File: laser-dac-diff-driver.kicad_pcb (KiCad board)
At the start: 2 copper layers, 51 parts, among them IC401 DCDC-CONV_TRACO_TMH-XXXX_Dual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, P101 CONN_2, P102 CONN_3X2, P103 CONN_6X2, U101 AD5689RARUZ, U102 74HC04, U201 OP470, U202 LM358, U401 LM317EMP, U402 LM317EMP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

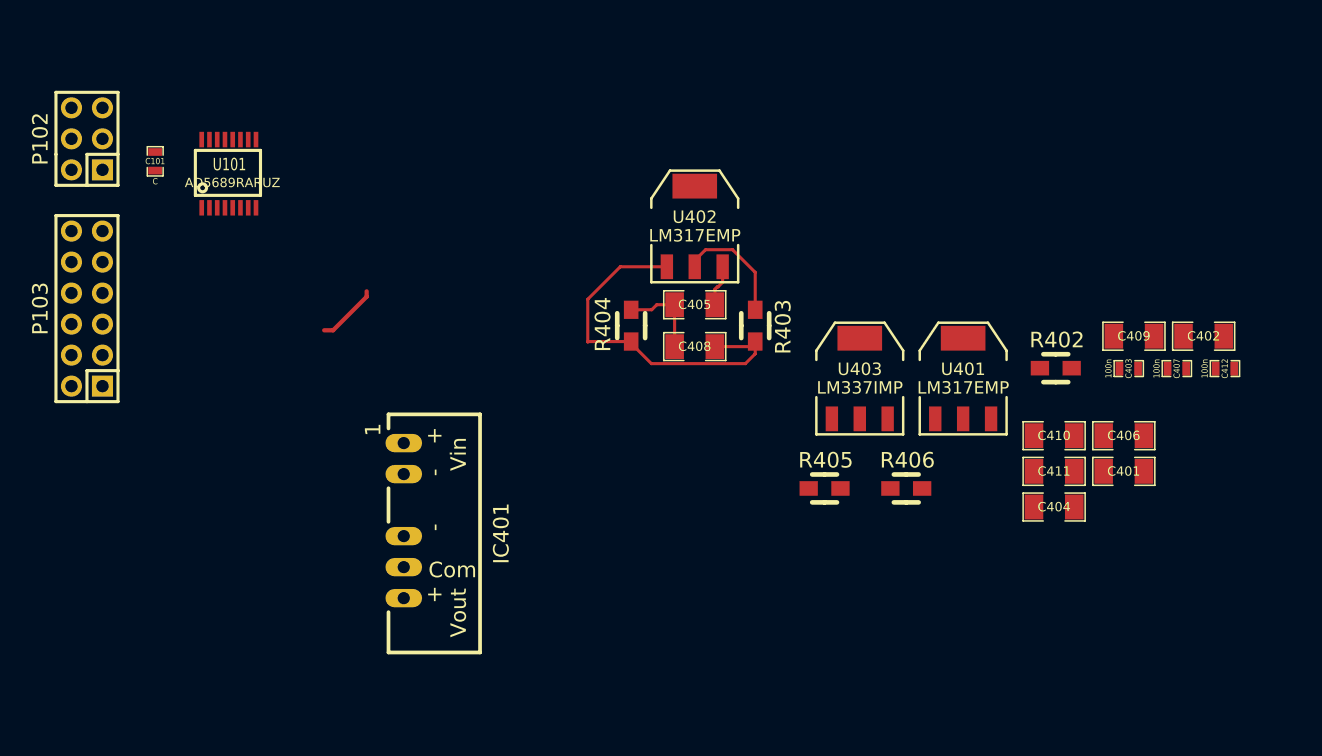
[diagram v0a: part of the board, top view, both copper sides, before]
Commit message: Power supply position changes
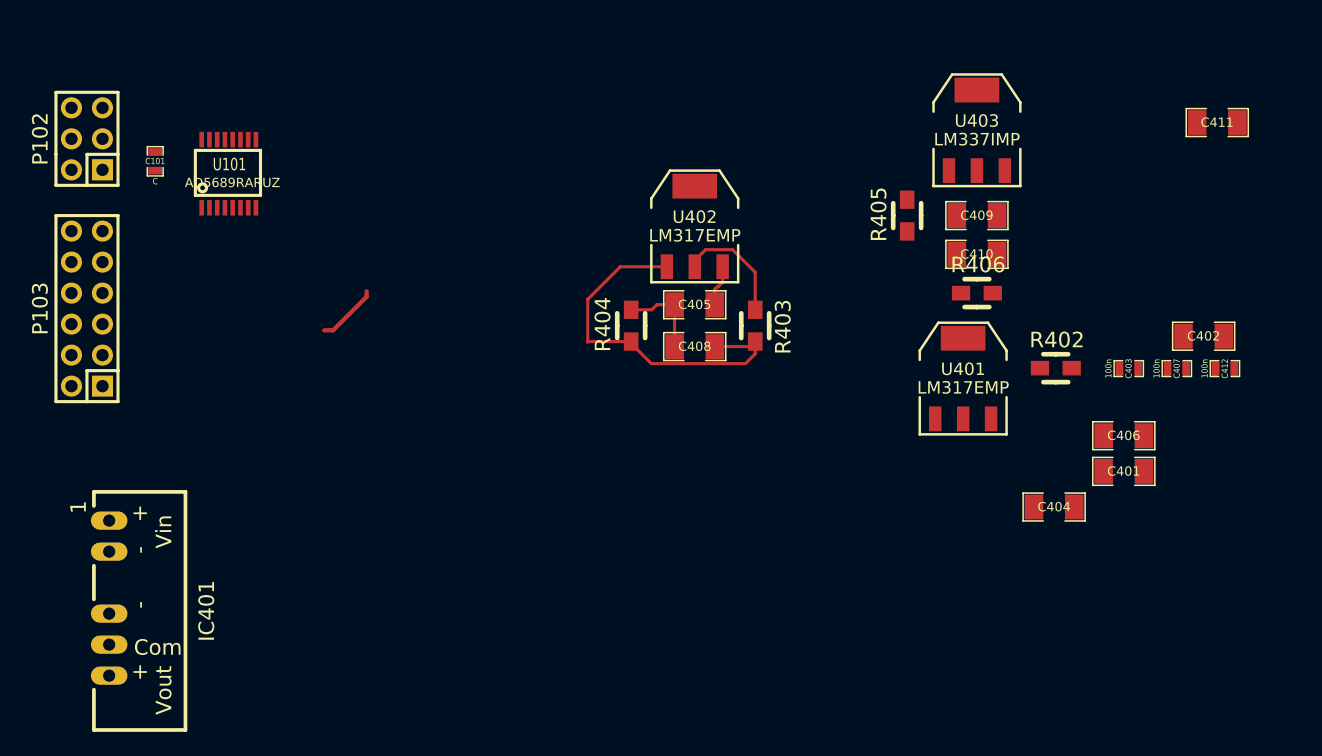
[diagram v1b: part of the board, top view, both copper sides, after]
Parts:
- moved C411 31.5 mm to (215.9, 94.0)
- moved IC401 25.0 mm to (127.6, 134.0)
- moved R405 23.4 mm to (190.5, 101.6), turned to 90 degrees
- moved U403 22.5 mm to (196.2, 94.6)
- moved R406 17.0 mm to (196.2, 108.0)
- moved C409 16.2 mm to (196.2, 101.6), turned to 180 degrees
- moved C410 16.1 mm to (196.2, 104.8)
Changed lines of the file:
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@@
     (pad_to_mask_clearance 0.2)
     (aux_axis_origin 0 0)
-    (visible_elements 7FFFFFFF)
+    (visible_elements 7FFFFFBF)
     (pcbplotparams
       (layerselection 3178497)
@@
   )
   (module SMD_Packages:SM1206 (layer F.Cu)
-    (at 209.077001 111.481501)
-    (attr smd)
-    (fp_text reference C409 (at 0 0) (layer F.SilkS)
-      (effects (font (size 0.762 0.762) (thickness 0.127)))
-    )
-    (fp_text value 10u (at 0 0) (layer F.SilkS) hide
+    (at 196.215 101.6 180)
+    (attr smd)
+    (fp_text reference C409 (at 0 0 180) (layer F.SilkS)
+      (effects (font (size 0.762 0.762) (thickness 0.127)))
+    )
+    (fp_text value 10u (at 0 0 180) (layer F.SilkS) hide
+      (effects (font (size 0.762 0.762) (thickness 0.127)))
+    )
+    (fp_line (start -2.54 -1.143) (end -2.54 1.143) (layer F.SilkS) (width 0.127))
+    (fp_line (start -2.54 1.143) (end -0.889 1.143) (layer F.SilkS) (width 0.127))
+    (fp_line (start 0.889 -1.143) (end 2.54 -1.143) (layer F.SilkS) (width 0.127))
+    (fp_line (start 2.54 -1.143) (end 2.54 1.143) (layer F.SilkS) (width 0.127))
+    (fp_line (start 2.54 1.143) (end 0.889 1.143) (layer F.SilkS) (width 0.127))
+    (fp_line (start -0.889 -1.143) (end -2.54 -1.143) (layer F.SilkS) (width 0.127))
+    (pad 1 smd rect (at -1.651 0 180) (size 1.524 2.032) (layers F.Cu F.Paste F.Mask)
+      (net 22 AGND))
+    (pad 2 smd rect (at 1.651 0 180) (size 1.524 2.032) (layers F.Cu F.Paste F.Mask)
+      (net 26 "Net-(C409-Pad2)"))
+    (model smd/chip_cms.wrl
+      (at (xyz 0 0 0))
+      (scale (xyz 0.17 0.16 0.16))
+      (rotate (xyz 0 0 0))
+    )
+  )
+  (module SMD_Packages:SM1206 (layer F.Cu)
+    (at 196.215 104.775)
+    (attr smd)
+    (fp_text reference C410 (at 0 0) (layer F.SilkS)
+      (effects (font (size 0.762 0.762) (thickness 0.127)))
+    )
+    (fp_text value 1u (at 0 0) (layer F.SilkS) hide
       (effects (font (size 0.762 0.762) (thickness 0.127)))
     )
@@
       (net 22 AGND))
     (pad 2 smd rect (at 1.651 0) (size 1.524 2.032) (layers F.Cu F.Paste F.Mask)
-      (net 26 "Net-(C409-Pad2)"))
+      (net 27 "Net-(C410-Pad2)"))
     (model smd/chip_cms.wrl
       (at (xyz 0 0 0))
@@
   )
   (module SMD_Packages:SM1206 (layer F.Cu)
-    (at 202.537001 119.631501)
-    (attr smd)
-    (fp_text reference C410 (at 0 0) (layer F.SilkS)
+    (at 215.9 93.98)
+    (attr smd)
+    (fp_text reference C411 (at 0 0) (layer F.SilkS)
       (effects (font (size 0.762 0.762) (thickness 0.127)))
     )
@@
       (net 22 AGND))
     (pad 2 smd rect (at 1.651 0) (size 1.524 2.032) (layers F.Cu F.Paste F.Mask)
-      (net 27 "Net-(C410-Pad2)"))
-    (model smd/chip_cms.wrl
-      (at (xyz 0 0 0))
-      (scale (xyz 0.17 0.16 0.16))
-      (rotate (xyz 0 0 0))
-    )
-  )
-  (module SMD_Packages:SM1206 (layer F.Cu)
-    (at 202.537001 122.551501)
-    (attr smd)
-    (fp_text reference C411 (at 0 0) (layer F.SilkS)
-      (effects (font (size 0.762 0.762) (thickness 0.127)))
-    )
-    (fp_text value 1u (at 0 0) (layer F.SilkS) hide
-      (effects (font (size 0.762 0.762) (thickness 0.127)))
-    )
-    (fp_line (start -2.54 -1.143) (end -2.54 1.143) (layer F.SilkS) (width 0.127))
-    (fp_line (start -2.54 1.143) (end -0.889 1.143) (layer F.SilkS) (width 0.127))
-    (fp_line (start 0.889 -1.143) (end 2.54 -1.143) (layer F.SilkS) (width 0.127))
-    (fp_line (start 2.54 -1.143) (end 2.54 1.143) (layer F.SilkS) (width 0.127))
-    (fp_line (start 2.54 1.143) (end 0.889 1.143) (layer F.SilkS) (width 0.127))
-    (fp_line (start -0.889 -1.143) (end -2.54 -1.143) (layer F.SilkS) (width 0.127))
-    (pad 1 smd rect (at -1.651 0) (size 1.524 2.032) (layers F.Cu F.Paste F.Mask)
-      (net 22 AGND))
-    (pad 2 smd rect (at 1.651 0) (size 1.524 2.032) (layers F.Cu F.Paste F.Mask)
       (net 3 -VAA))
     (model smd/chip_cms.wrl
@@
   )
   (module DCDCs:DCDC-Conv_TRACO_TMH-xxxx_Dual_RevA_27Mar2011 (layer F.Cu)
-    (at 151.765 127.635 270)
+    (at 127.635 133.985 270)
     (descr "DCDC-Converter, TRACO, TMH-xxxx, Dual output, RevA, 27Mar2011")
     (tags "DCDC-Converter, TRACO, TMH-xxxx, Dual output, RevA, 27Mar2011")
@@
   )
   (module Resistors_SMD:Resistor_SMD0805_HandSoldering (layer F.Cu)
-    (at 183.735983 123.95024)
-    (descr "Resistor, SMD, 0805, Hand soldering,")
-    (tags "Resistor, SMD, 0805, Hand soldering,")
-    (attr smd)
-    (fp_text reference R405 (at 0.09906 -2.30124) (layer F.SilkS)
-      (effects (font (thickness 0.3048)))
-    )
-    (fp_text value 1k8 (at 0.20066 2.60096) (layer F.SilkS) hide
-      (effects (font (thickness 0.3048)))
-    )
-    (fp_line (start 0 -1.143) (end -1.016 -1.143) (layer F.SilkS) (width 0.381))
-    (fp_line (start 0 -1.143) (end 1.016 -1.143) (layer F.SilkS) (width 0.381))
-    (fp_line (start 0 1.143) (end -1.016 1.143) (layer F.SilkS) (width 0.381))
-    (fp_line (start 0 1.143) (end 1.016 1.143) (layer F.SilkS) (width 0.381))
-    (pad 1 smd rect (at -1.30048 0) (size 1.50114 1.19888) (layers F.Cu F.Paste F.Mask)
-      (net 22 AGND))
-    (pad 2 smd rect (at 1.30048 0) (size 1.50114 1.19888) (layers F.Cu F.Paste F.Mask)
+    (at 190.5 101.6 90)
+    (descr "Resistor, SMD, 0805, Hand soldering,")
+    (tags "Resistor, SMD, 0805, Hand soldering,")
+    (attr smd)
+    (fp_text reference R405 (at 0.09906 -2.30124 90) (layer F.SilkS)
+      (effects (font (thickness 0.3048)))
+    )
+    (fp_text value 1k8 (at 0.20066 2.60096 90) (layer F.SilkS) hide
+      (effects (font (thickness 0.3048)))
+    )
+    (fp_line (start 0 -1.143) (end -1.016 -1.143) (layer F.SilkS) (width 0.381))
+    (fp_line (start 0 -1.143) (end 1.016 -1.143) (layer F.SilkS) (width 0.381))
+    (fp_line (start 0 1.143) (end -1.016 1.143) (layer F.SilkS) (width 0.381))
+    (fp_line (start 0 1.143) (end 1.016 1.143) (layer F.SilkS) (width 0.381))
+    (pad 1 smd rect (at -1.30048 0 90) (size 1.50114 1.19888) (layers F.Cu F.Paste F.Mask)
+      (net 22 AGND))
+    (pad 2 smd rect (at 1.30048 0 90) (size 1.50114 1.19888) (layers F.Cu F.Paste F.Mask)
       (net 26 "Net-(C409-Pad2)"))
   )
   (module Resistors_SMD:Resistor_SMD0805_HandSoldering (layer F.Cu)
-    (at 190.425983 123.95024)
+    (at 196.215 107.95)
     (descr "Resistor, SMD, 0805, Hand soldering,")
     (tags "Resistor, SMD, 0805, Hand soldering,")
@@
   )
   (module SMD_Packages:SOT223 (layer F.Cu)
-    (at 186.618814 114.948601)
+    (at 196.215 94.615)
     (descr "module CMS SOT223 4 pins")
     (tags "CMS SOT")

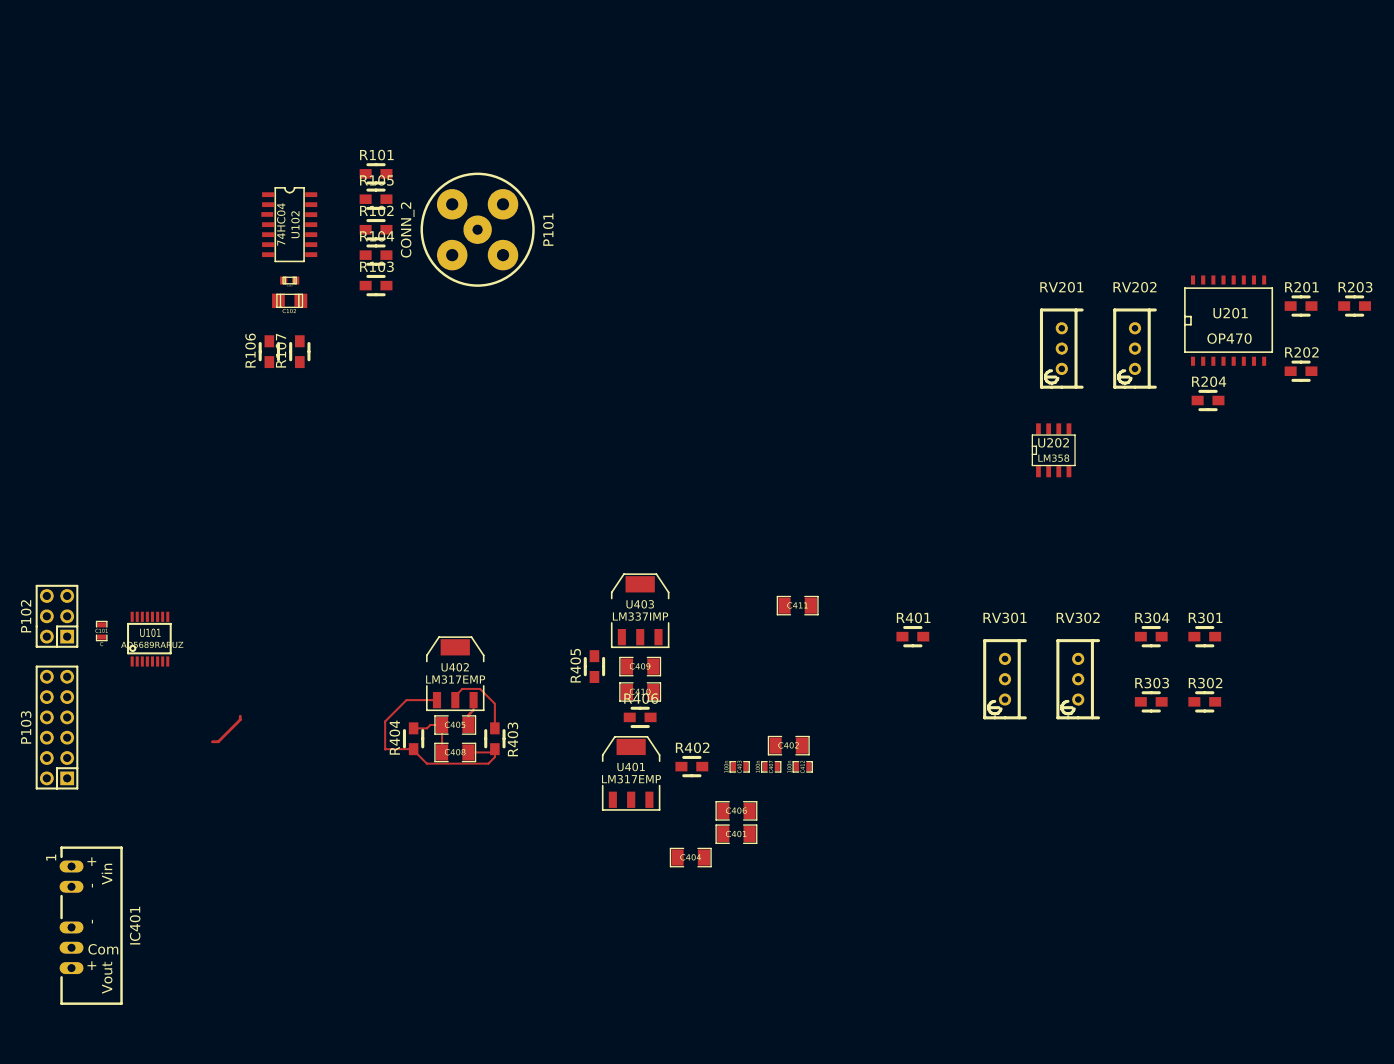
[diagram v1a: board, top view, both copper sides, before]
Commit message: Sorted out more component positions
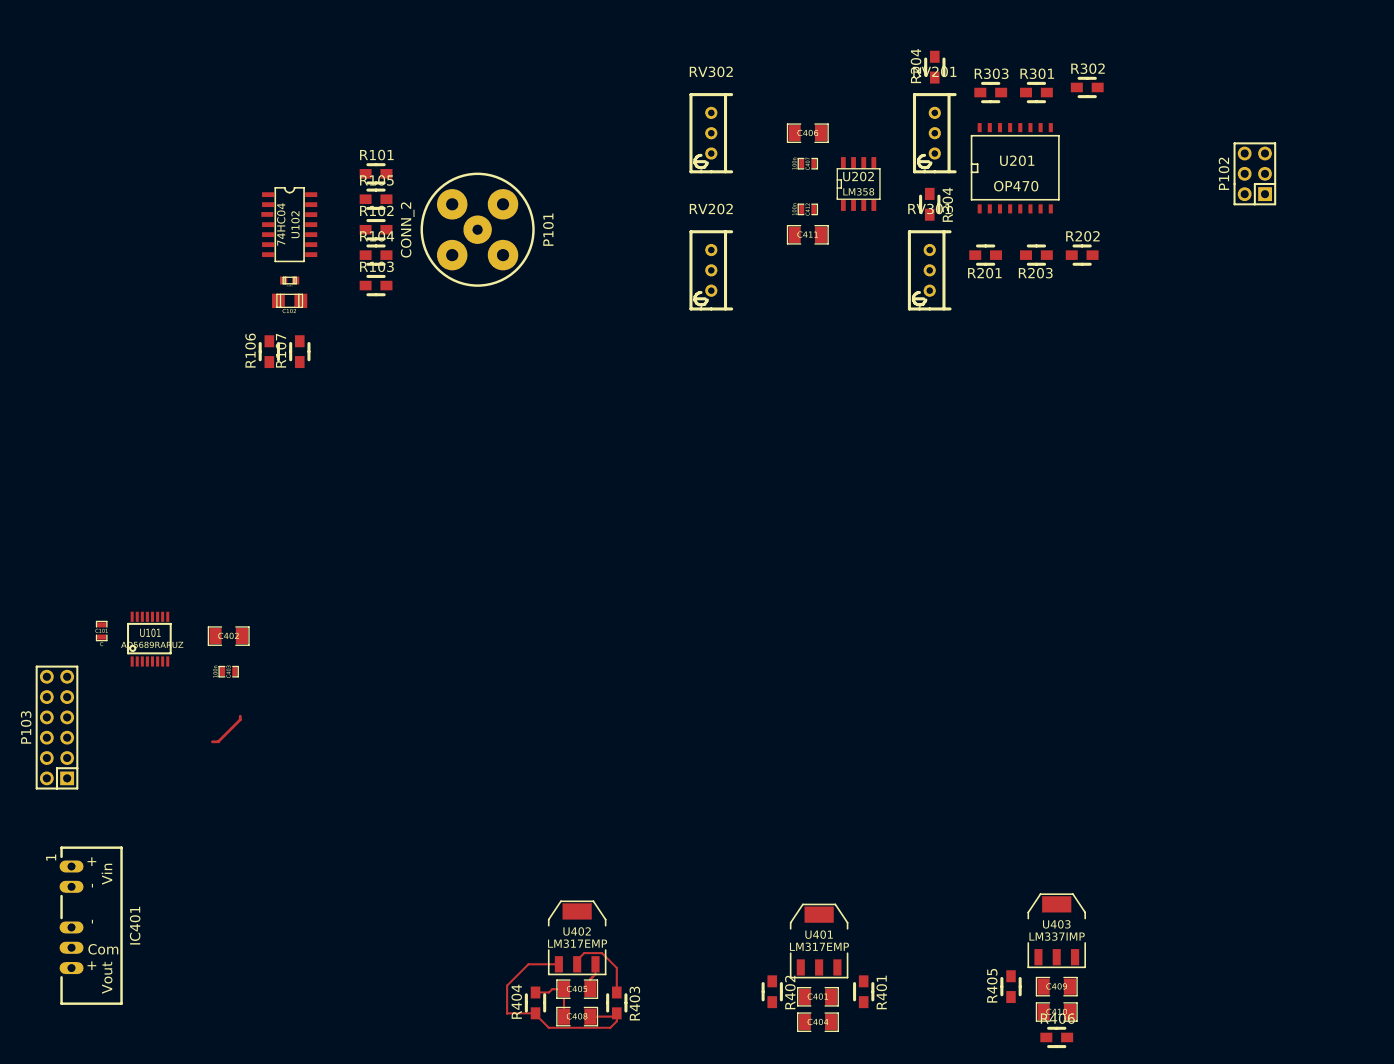
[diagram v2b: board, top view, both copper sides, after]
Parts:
- moved P102 159.6 mm to (273.1, 40.0)
- moved C406 85.2 mm to (217.2, 34.9)
- moved RV302 82.2 mm to (205.1, 34.9)
- moved R303 78.8 mm to (240.0, 29.8)
- moved R302 78.2 mm to (252.1, 29.2)
- moved C407 75.5 mm to (217.2, 38.7)
- moved C402 71.3 mm to (144.8, 97.8)
- moved R301 71.2 mm to (245.7, 29.8)
- moved C412 69.7 mm to (217.2, 44.5)
- moved C409 65.7 mm to (248.3, 141.6)
- moved C410 65.7 mm to (248.3, 144.8)
- moved R405 65.7 mm to (242.6, 141.6)
- moved R406 65.7 mm to (248.3, 148.0)
- moved U403 65.7 mm to (248.3, 134.6)
- moved C403 65.0 mm to (144.8, 102.2)
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
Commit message: Added extra small decoupling for reference. Pin-swapped and fixed pin numbers on digital input.
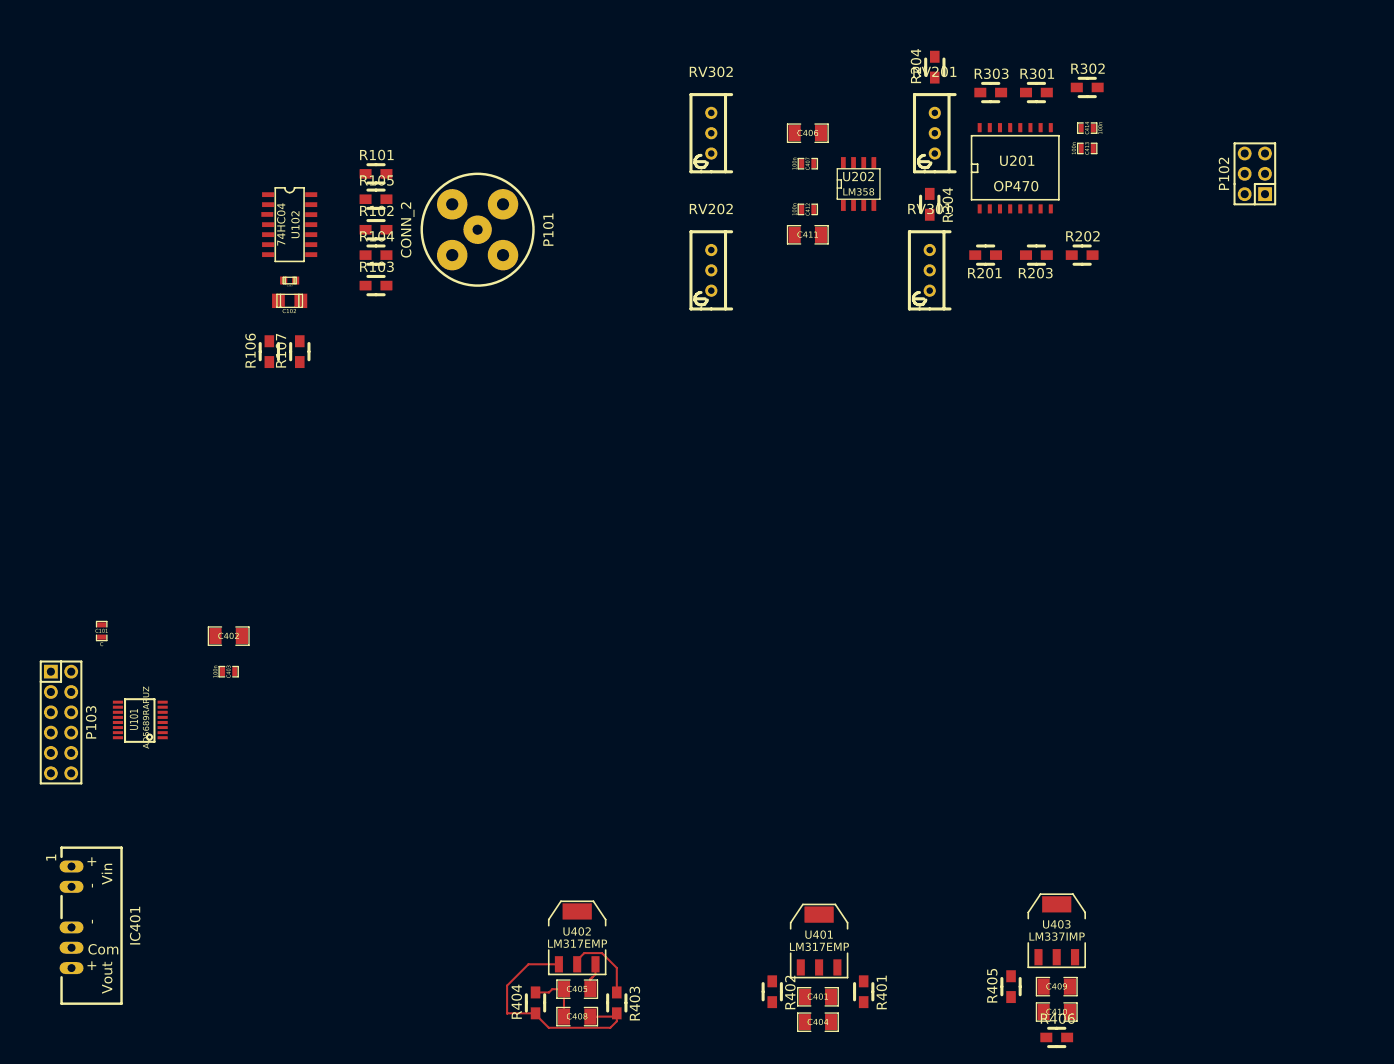
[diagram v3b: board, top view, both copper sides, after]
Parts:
- added C413: 100n, SMD_Packages:SM0603_Capa, F.Cu at (252.1, 36.8)
- added C414: 100n, SMD_Packages:SM0603_Capa, F.Cu at (252.1, 34.3)
- moved U101 10.3 mm to (136.5, 110.5), turned to 90 degrees
- moved P103 0.81 mm to (123.8, 108.6), turned to 270 degrees
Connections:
- net AGND renamed DGND
- P103 pad 10: /SCLK -> /SDIN
- P103 pad 12: /GAIN -> /~RESET
- P103 pad 3: /~LDAC -> /GAIN
- P103 pad 4: /~RESET -> /~LDAC
- P103 pad 6: /SDIN -> /SCLK
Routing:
- net (no net): track 5.06 -> 0.00 mm
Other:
- net class Power: trace_width 0.35 -> 0.5
- net class asdf added: clearance 0.254, trace_width 1, via_dia 0.889, via_drill 0.635
